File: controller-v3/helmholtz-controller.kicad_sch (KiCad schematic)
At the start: 57 parts, among them J1 Screw_Terminal_01x02, J2 Screw_Terminal_01x02, J3 Screw_Terminal_01x02, J4 Screw_Terminal_01x02, J5 Conn_01x04, U1 DRV8871DDA, U2 DRV8871DDA, U3 INA226, U4 INA226, U5 DRV8871DDA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

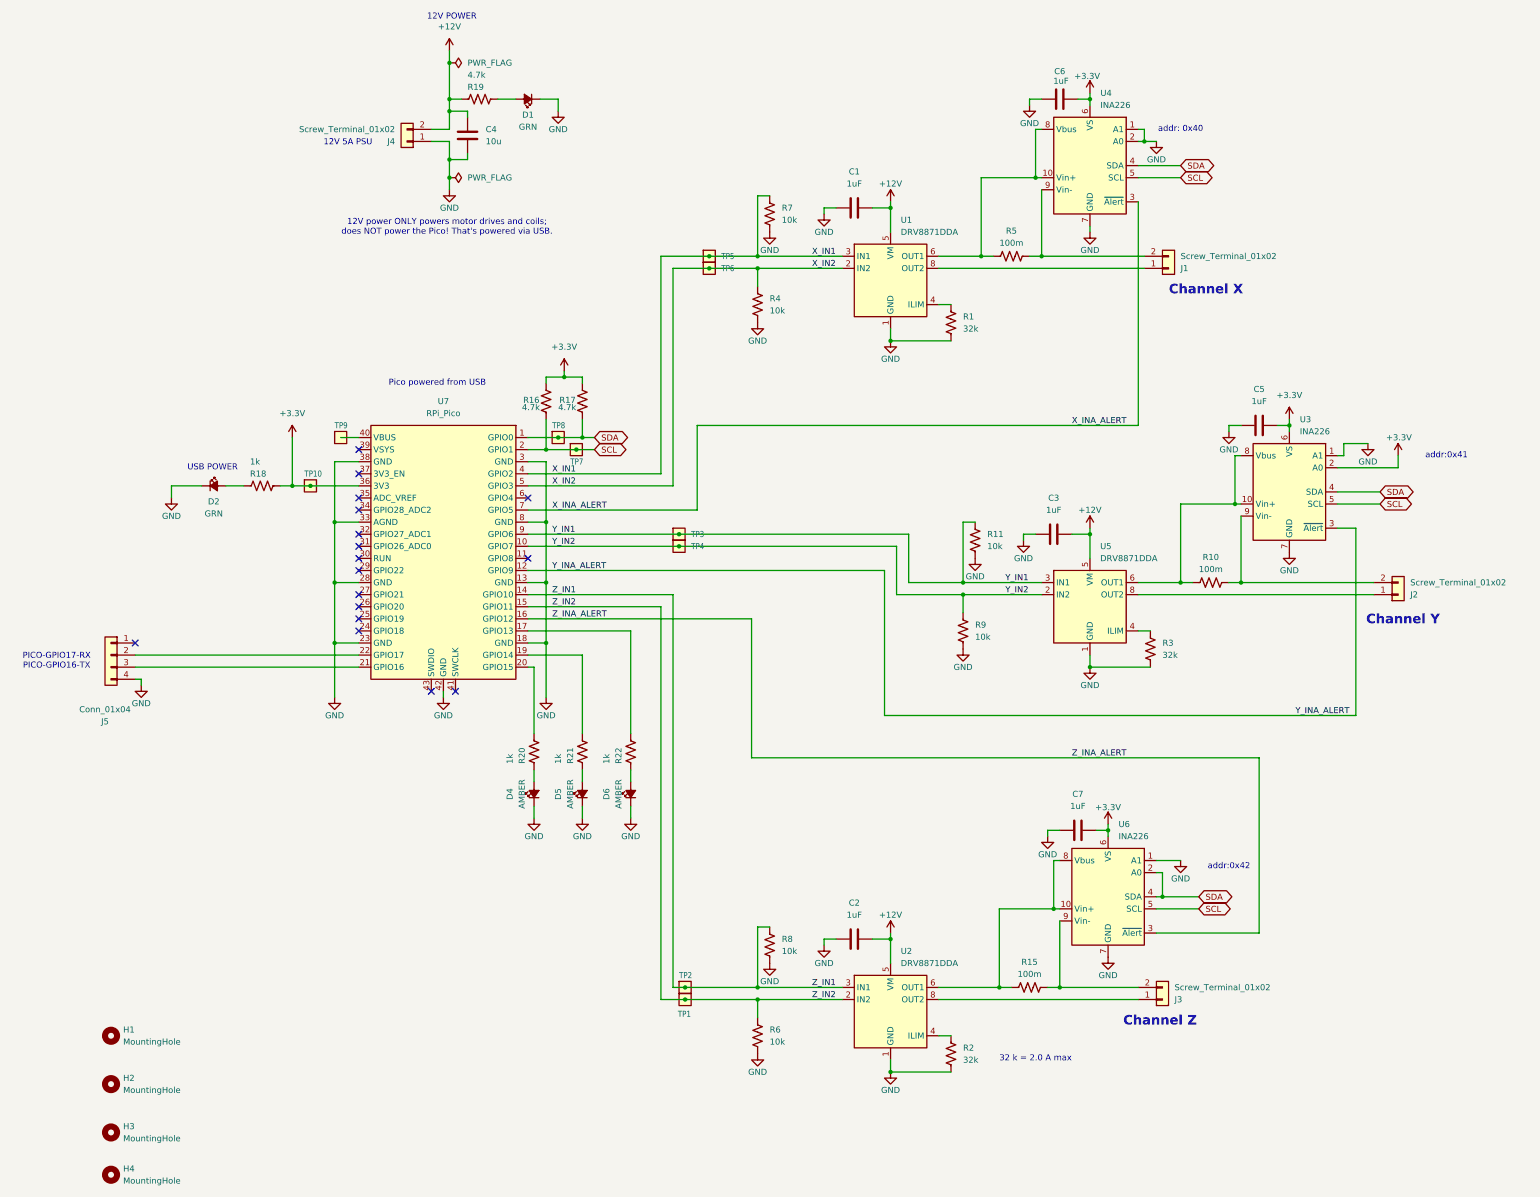
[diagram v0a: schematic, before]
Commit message: Helholtz cage controller v3.0, upgrade to KICad 10, new gitignore file
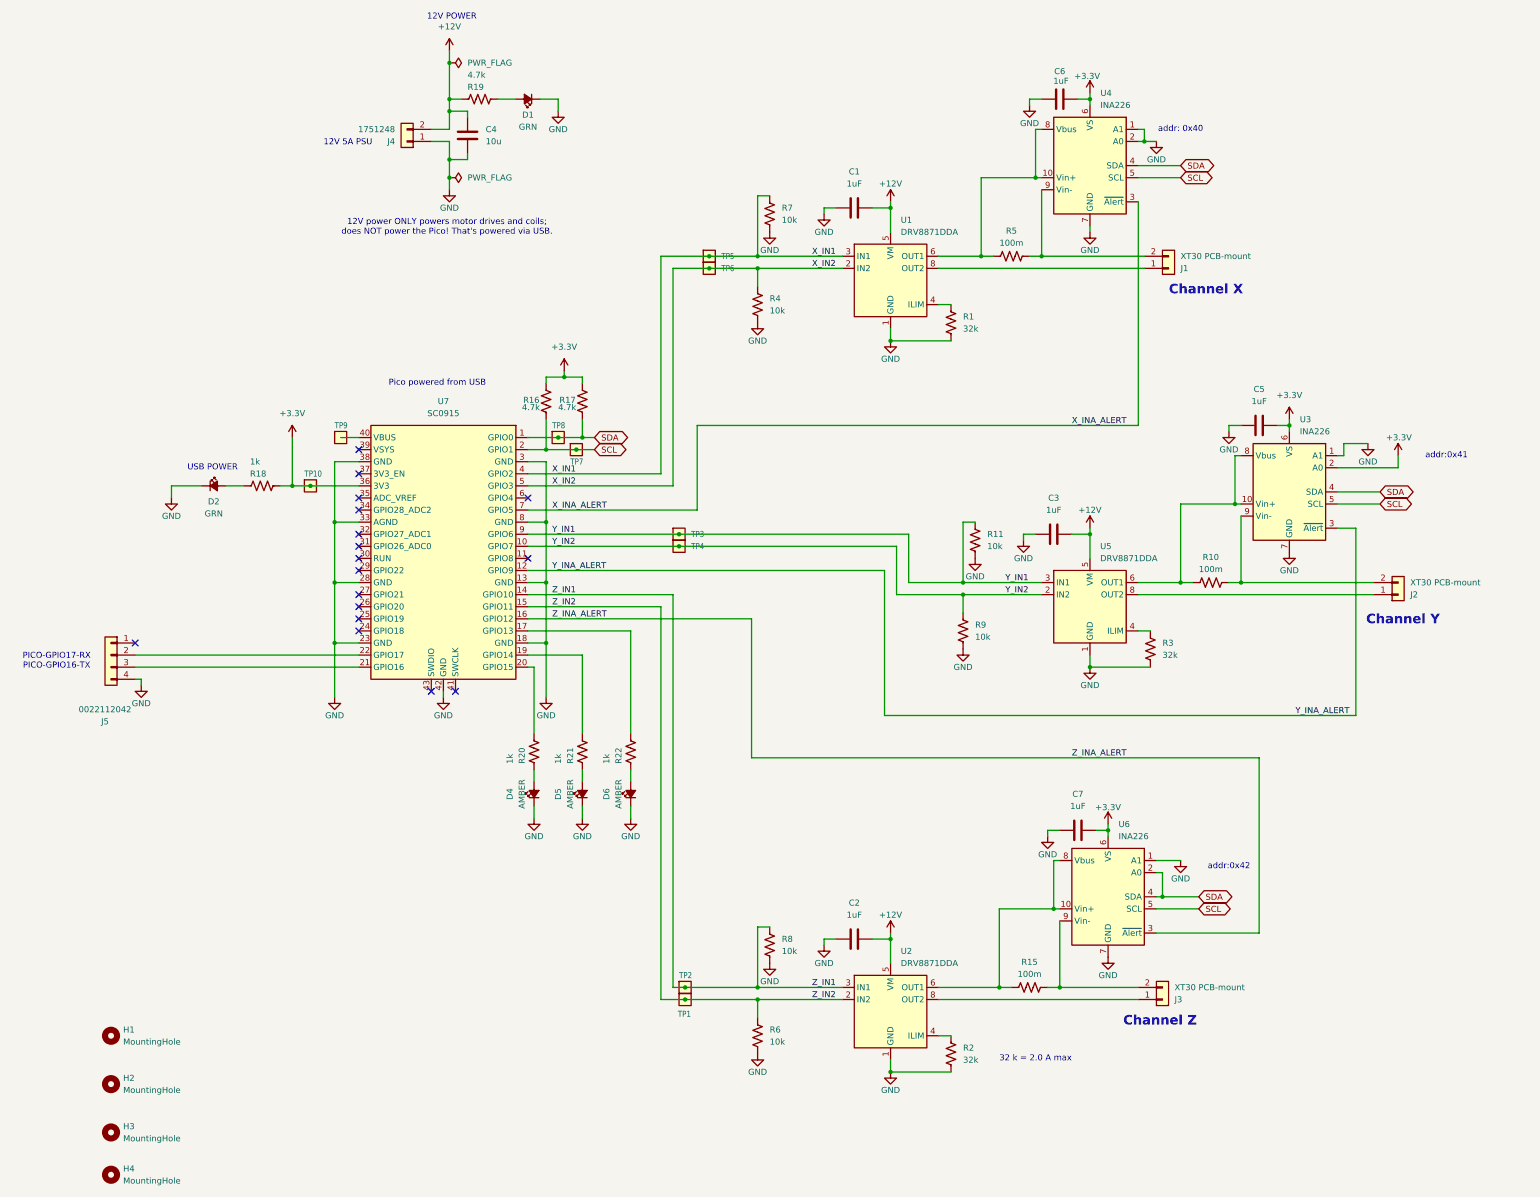
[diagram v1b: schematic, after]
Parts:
- J1, J2, J3: value Screw_Terminal_01x02 -> XT30 PCB-mount
- J4: value Screw_Terminal_01x02 -> 1751248
- J5: value Conn_01x04 -> 0022112042
- U3, U4, U6: footprint Package_SO:VSSOP-10_3x3mm_P0.5mm -> Package_SO:TSSOP-10_3x3mm_P0.5mm
- U7: value RPi_Pico -> SC0915
